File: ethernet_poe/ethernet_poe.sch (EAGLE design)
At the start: 22 parts, among them U1 W5500

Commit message: Added 5V Regulator
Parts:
- added C7: 220 nF, rcl:C-USC0603
- added C8: 22 nF, rcl:C-USC0603
- added D1: (no value), RoboJackets-Diodes:SCHOTTKYSOD-323
- added L1: 47 uH, RoboJackets-Inductors:744771147
- added R14: 22k, rcl:R-US_R0603
- added U2: IFX91041, RoboJackets-PowerICs:IFX91041
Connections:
- new net +5V: L1.P$1, U2.FB
- new net N$14: C7.2, D1.C, L1.P$2, U2.BUO
- new net N$15: C7.1, U2.BDS
- new net N$16: C8.2, R14.1
- new net N$17: C8.1, U2.COMP
- net +24V: now also U2.EN, U2.VS
- net GND: now also D1.A, R14.2, U2.GND, U2.SYNC
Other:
- moved on the sheet: C1, C2, C3, C6, R1, R10, R11, R12, R13, R2, R9, U$1

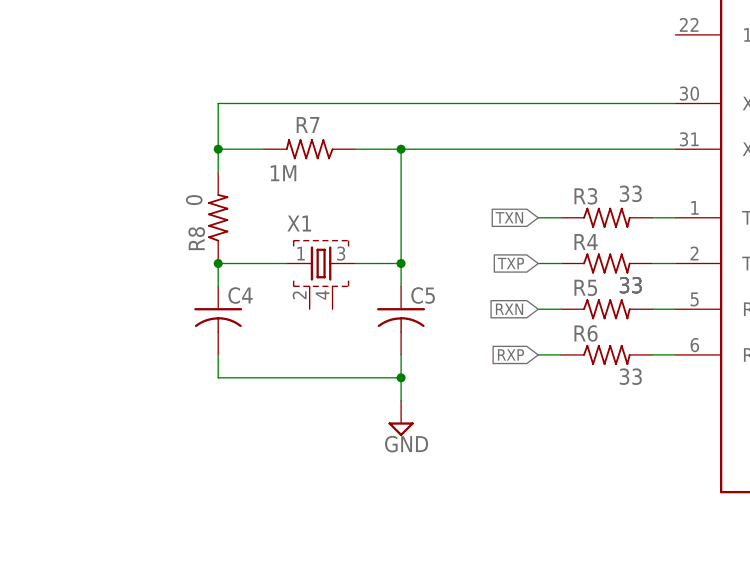
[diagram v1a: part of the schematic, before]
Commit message: Cleaned up schematic, added inductor to library
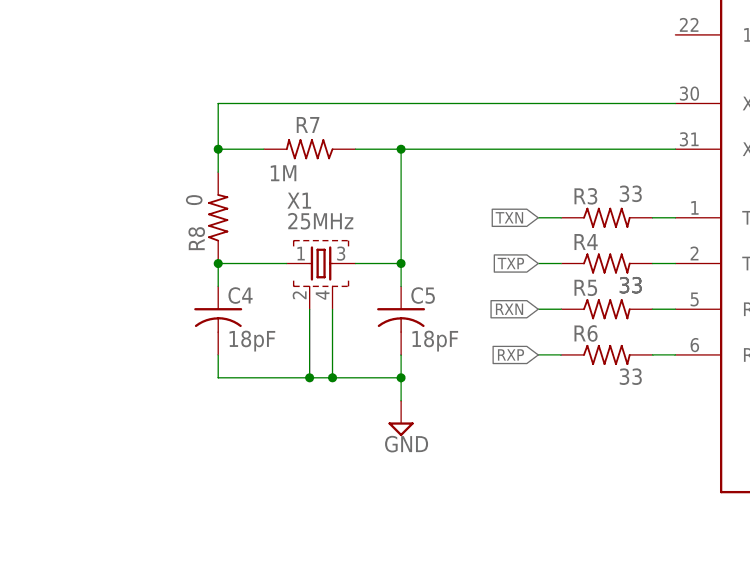
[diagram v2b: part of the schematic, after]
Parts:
- C4, C5: value (none) -> 18pF
- X1: value (none) -> 25MHz
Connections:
- net GND: now also X1.SHD1, X1.SHD2
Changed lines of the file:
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@@
 <part name="U1" library="ethernet_poe" deviceset="W5500" device=""/>
 <part name="U$1" library="ethernet_poe" deviceset="ARJP11A" device=""/>
-<part name="X1" library="ethernet_poe" deviceset="ABM10W-25.0000MHZ-6-K1Z-T3" device=""/>
+<part name="X1" library="ethernet_poe" deviceset="ABM10W-25.0000MHZ-6-K1Z-T3" device="" value="25MHz"/>
 <part name="C1" library="rcl" library_urn="urn:adsk.eagle:library:334" deviceset="C-US" device="C0603" package3d_urn="urn:adsk.eagle:package:23616/2" value="6.8nF"/>
 <part name="C2" library="rcl" library_urn="urn:adsk.eagle:library:334" deviceset="C-US" device="C0603" package3d_urn="urn:adsk.eagle:package:23616/2" value="6.8nF"/>
@@
 <part name="R5" library="rcl" library_urn="urn:adsk.eagle:library:334" deviceset="R-US_" device="R0603" package3d_urn="urn:adsk.eagle:package:23555/3" value="33"/>
 <part name="R6" library="rcl" library_urn="urn:adsk.eagle:library:334" deviceset="R-US_" device="R0603" package3d_urn="urn:adsk.eagle:package:23555/3" value="33"/>
-<part name="C4" library="rcl" library_urn="urn:adsk.eagle:library:334" deviceset="C-US" device="C0603" package3d_urn="urn:adsk.eagle:package:23616/2"/>
-<part name="C5" library="rcl" library_urn="urn:adsk.eagle:library:334" deviceset="C-US" device="C0603" package3d_urn="urn:adsk.eagle:package:23616/2"/>
+<part name="C4" library="rcl" library_urn="urn:adsk.eagle:library:334" deviceset="C-US" device="C0603" package3d_urn="urn:adsk.eagle:package:23616/2" value="18pF"/>
+<part name="C5" library="rcl" library_urn="urn:adsk.eagle:library:334" deviceset="C-US" device="C0603" package3d_urn="urn:adsk.eagle:package:23616/2" value="18pF"/>
 <part name="SUPPLY2" library="supply2" library_urn="urn:adsk.eagle:library:372" deviceset="GND" device=""/>
 <part name="R8" library="rcl" library_urn="urn:adsk.eagle:library:334" deviceset="R-US_" device="R0603" package3d_urn="urn:adsk.eagle:package:23555/3" value="0"/>
@@
 </instance>
 <instance part="X1" gate="G$1" x="50.8" y="60.96" smashed="yes">
-<attribute name="NAME" x="48.26" y="64.516" size="1.778" layer="95" font="vector"/>
+<attribute name="NAME" x="48.26" y="67.056" size="1.778" layer="95" font="vector"/>
 <attribute name="VALUE" x="48.26" y="64.77" size="1.778" layer="96" font="vector"/>
 </instance>
@@
 <pinref part="C4" gate="G$1" pin="2"/>
 <wire x1="40.64" y1="50.8" x2="40.64" y2="48.26" width="0.1524" layer="91"/>
-<wire x1="40.64" y1="48.26" x2="60.96" y2="48.26" width="0.1524" layer="91"/>
+<wire x1="40.64" y1="48.26" x2="50.8" y2="48.26" width="0.1524" layer="91"/>
 <pinref part="C5" gate="G$1" pin="2"/>
+<wire x1="50.8" y1="48.26" x2="53.34" y2="48.26" width="0.1524" layer="91"/>
+<wire x1="53.34" y1="48.26" x2="60.96" y2="48.26" width="0.1524" layer="91"/>
 <wire x1="60.96" y1="48.26" x2="60.96" y2="50.8" width="0.1524" layer="91"/>
 <pinref part="SUPPLY2" gate="GND" pin="GND"/>
 <wire x1="60.96" y1="45.72" x2="60.96" y2="48.26" width="0.1524" layer="91"/>
 <junction x="60.96" y="48.26"/>
-</segment>
-<segment>
+<pinref part="X1" gate="G$1" pin="SHD1"/>
+<wire x1="50.8" y1="55.88" x2="50.8" y2="48.26" width="0.1524" layer="91"/>
+<junction x="50.8" y="48.26"/>
+<pinref part="X1" gate="G$1" pin="SHD2"/>
+<wire x1="53.34" y1="55.88" x2="53.34" y2="48.26" width="0.1524" layer="91"/>
+<junction x="53.34" y="48.26"/>
+</segment>
+<segment>

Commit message: Added Regulators and 3v3 D,A
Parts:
- added C10: 10nF, rcl:C-USC0603
- added C9: 4.7uF, rcl:C-USC0603
- added D2, D3, D4: GRN, led:LEDCHIP-LED0603
- added R15, R16, R17: 4.9k, rcl:R-US_R0603
- added R18: 12.4k 1%, rcl:R-US_R0603
- added R19: 4.7k, rcl:R-US_R0603
- added R20: 600, rcl:R-US_R0603
- added R21: 200, rcl:R-US_R0603
- added U3: AZ1117EH-3.3TRG1, ethernet_poe:AZ1117EH-3.3TRG1
- R1, R10, R11, R2, R9: value 49 -> 49 1%
- renumbered U$1 to J1
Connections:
- new net !INTN: R16.2, U1.!INTN
- new net !RSTN: R17.1, U1.!RSTN
- new net !SCSN: R15.2, U1.!SCSN
- new net +3V3_A: R10.2, R11.2, R9.2
- new net +3V3_D: J1.GLED+, J1.YLED+, R15.1, R16.1, R17.2, R21.1, U1.PMODE0, U1.PMODE1, U1.PMODE2, U1.VDD, U3.OUT
- new net MISO: U1.MISO
- new net MOSI: U1.MOSI
- new net N$18: C10.1, U1.1V2O
- new net N$19: C9.1, U1.TOCAP
- new net N$20: D2.A, R19.2
- new net N$21: R18.2, U1.EXRES1
- new net N$22: D4.A, R21.2
- new net N$24: D3.A, R20.2
- new net SCLK: U1.SCLK
- net +24V: now also R19.1
- net +3V3: now also U1.AVDD; no longer J1.GLED+, J1.YLED+, R10.2, R11.2, R9.2
- net +5V: now also R20.1, U3.IN
- net GND: now also C10.2, C9.2, D2.C, D3.C, D4.C, R18.1, U1.AGND, U1.GND, U1.RSVD1, U1.RSVD2, U1.RSVD3, U1.RSVD4, U1.RSVD5, U1.RSVD6, U3.ADJ/GND

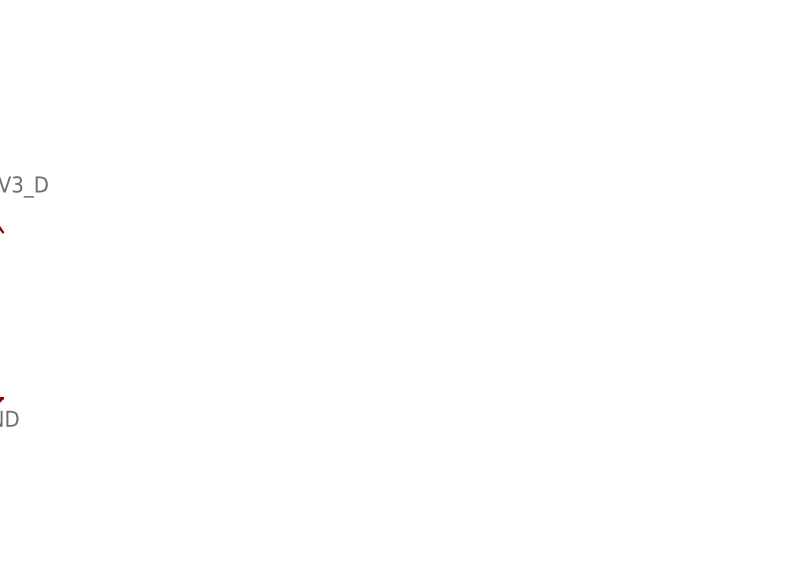
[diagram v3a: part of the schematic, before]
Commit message: Added inductor to schematic, fixed 3v3A/D
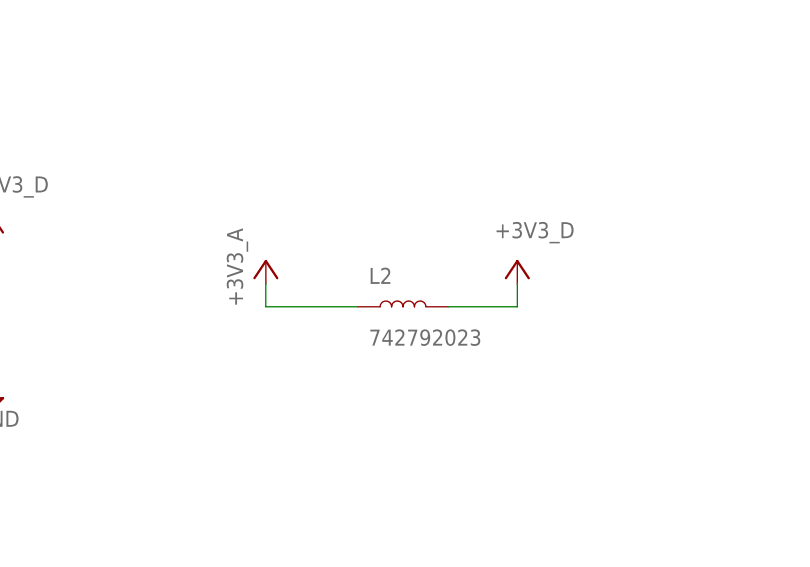
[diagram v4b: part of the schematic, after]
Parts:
- added L2: 742792023, ethernet_poe:INDUCTOR_0805
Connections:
- removed net +3V3: U1.AVDD
- net +3V3_A: now also L2.1, U1.AVDD
- net +3V3_D: now also L2.2

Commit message: Cleaned up style
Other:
- note added: "Control"
- note added: "Ethernet"
- note added: "LEDs"
- note added: "Power"
- moved on the sheet: C1, C10, C2, C3, C4, C5, C6, C9, D2, D3, D4, J1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

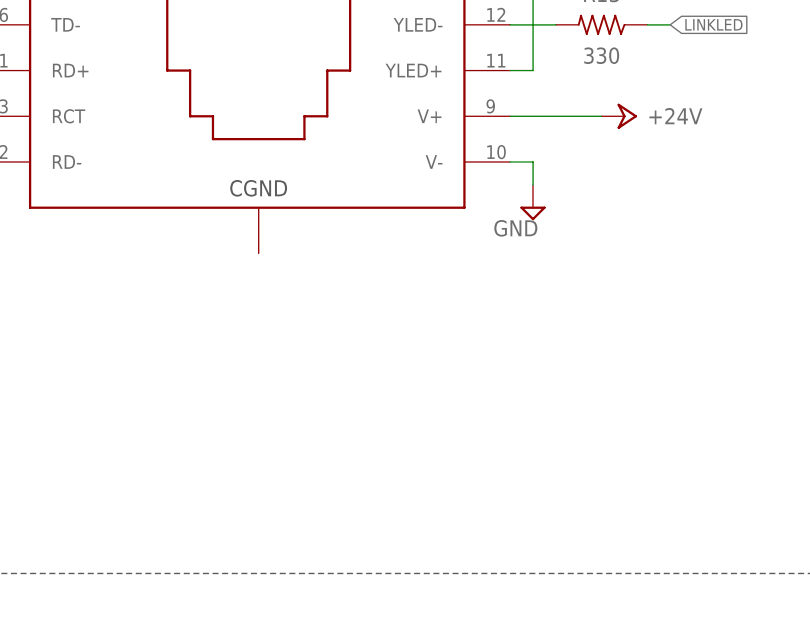
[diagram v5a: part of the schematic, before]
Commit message: Added chassis ground/shielding to ethernet
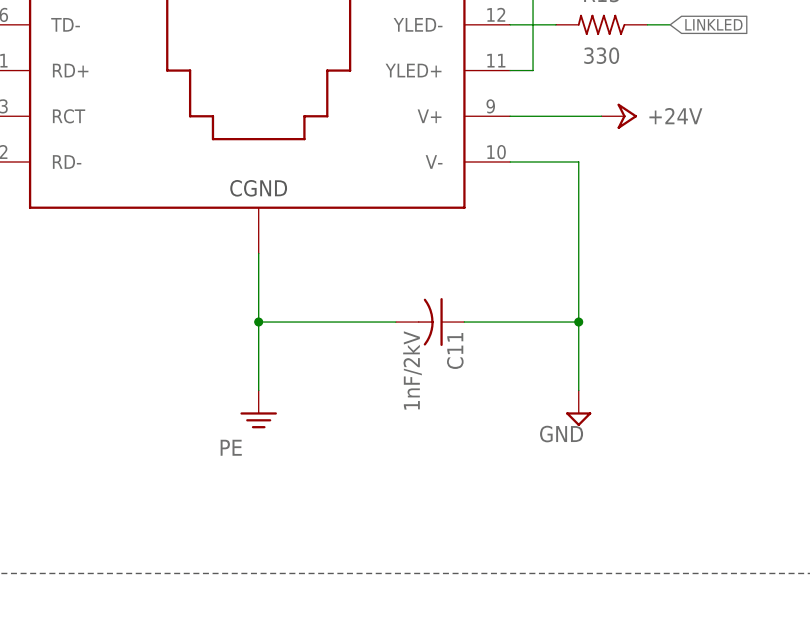
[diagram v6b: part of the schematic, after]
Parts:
- added C11: 1nF/2kV, rcl:C-USC1206
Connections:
- new net PE: C11.2, J1.CGND
- net GND: now also C11.1
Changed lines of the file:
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@@
 <part name="+3V3_A3" library="ethernet_poe" deviceset="+3V3_A" device=""/>
 <part name="+3V3_D4" library="ethernet_poe" deviceset="+3V3_D" device=""/>
+<part name="C11" library="rcl" library_urn="urn:adsk.eagle:library:334" deviceset="C-US" device="C1206" package3d_urn="urn:adsk.eagle:package:23618/2" value="1nF/2kV"/>
+<part name="SUPPLY13" library="supply2" library_urn="urn:adsk.eagle:library:372" deviceset="PE" device=""/>
 </parts>
 <sheets>
@@
 <attribute name="VALUE" x="388.62" y="205.74" size="1.778" layer="96" font="vector" align="center-left"/>
 </instance>
-<instance part="SUPPLY4" gate="GND" x="375.92" y="195.58" smashed="yes">
-<attribute name="VALUE" x="374.015" y="192.405" size="1.778" layer="96" font="vector" align="bottom-center"/>
+<instance part="SUPPLY4" gate="GND" x="381" y="172.72" smashed="yes">
+<attribute name="VALUE" x="379.095" y="169.545" size="1.778" layer="96" font="vector" align="bottom-center"/>
 </instance>
 <instance part="U2" gate="G$1" x="48.26" y="233.68" smashed="yes">
@@
 <instance part="+3V3_D4" gate="G$1" x="127" y="180.34" smashed="yes">
 <attribute name="VALUE" x="127" y="182.88" size="1.778" layer="96" font="vector" align="bottom-center"/>
+</instance>
+<instance part="C11" gate="G$1" x="365.76" y="182.88" smashed="yes" rot="R270">
+<attribute name="NAME" x="366.395" y="181.864" size="1.778" layer="95" font="vector" rot="R270"/>
+<attribute name="VALUE" x="361.569" y="181.864" size="1.778" layer="96" font="vector" rot="R270"/>
+</instance>
+<instance part="SUPPLY13" gate="PE" x="345.44" y="172.72" smashed="yes">
+<attribute name="VALUE" x="340.995" y="168.021" size="1.778" layer="96"/>
 </instance>
 </instances>
@@
 <pinref part="J1" gate="G$1" pin="V-"/>
 <pinref part="SUPPLY4" gate="GND" pin="GND"/>
-<wire x1="373.38" y1="200.66" x2="375.92" y2="200.66" width="0.1524" layer="91"/>
-<wire x1="375.92" y1="200.66" x2="375.92" y2="198.12" width="0.1524" layer="91"/>
+<wire x1="373.38" y1="200.66" x2="381" y2="200.66" width="0.1524" layer="91"/>
+<wire x1="381" y1="200.66" x2="381" y2="182.88" width="0.1524" layer="91"/>
+<pinref part="C11" gate="G$1" pin="1"/>
+<wire x1="381" y1="182.88" x2="381" y2="175.26" width="0.1524" layer="91"/>
+<wire x1="368.3" y1="182.88" x2="381" y2="182.88" width="0.1524" layer="91"/>
+<junction x="381" y="182.88"/>
 </segment>
 <segment>
@@
 </segment>
 </net>
+<net name="PE" class="0">
+<segment>
+<pinref part="J1" gate="G$1" pin="CGND"/>
+<pinref part="SUPPLY13" gate="PE" pin="PE"/>
+<wire x1="345.44" y1="190.5" x2="345.44" y2="182.88" width="0.1524" layer="91"/>
+<pinref part="C11" gate="G$1" pin="2"/>
+<wire x1="345.44" y1="182.88" x2="345.44" y2="175.26" width="0.1524" layer="91"/>
+<wire x1="360.68" y1="182.88" x2="345.44" y2="182.88" width="0.1524" layer="91"/>
+<junction x="345.44" y="182.88"/>
+</segment>
+</net>

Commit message: Began routing, clarified nets
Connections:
- net N$1 renamed RD+
- net N$2 renamed TCT
- net N$20 renamed 24V_LED
- net N$22 renamed 3V3_LED
- net N$24 renamed 5V_LED
- net N$3 renamed RD-
- net N$6 renamed RCT
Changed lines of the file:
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@@
 </segment>
 </net>
-<net name="N$2" class="0">
+<net name="TCT" class="0">
 <segment>
 <pinref part="J1" gate="G$1" pin="TCT"/>
@@
 </segment>
 </net>
-<net name="N$1" class="0">
+<net name="RD+" class="0">
 <segment>
 <pinref part="J1" gate="G$1" pin="RD+"/>
@@
 </segment>
 </net>
-<net name="N$3" class="0">
+<net name="RD-" class="0">
 <segment>
 <pinref part="J1" gate="G$1" pin="RD-"/>
@@
 </segment>
 </net>
-<net name="N$6" class="0">
+<net name="RCT" class="0">
 <segment>
 <pinref part="J1" gate="G$1" pin="RCT"/>
@@
 </segment>
 </net>
-<net name="N$20" class="0">
+<net name="24V_LED" class="0">
 <segment>
 <pinref part="R19" gate="G$1" pin="2"/>
@@
 </segment>
 </net>
-<net name="N$24" class="0">
+<net name="5V_LED" class="0">
 <segment>
 <pinref part="R20" gate="G$1" pin="2"/>
@@
 </segment>
 </net>
-<net name="N$22" class="0">
+<net name="3V3_LED" class="0">
 <segment>
 <pinref part="R21" gate="G$1" pin="2"/>
